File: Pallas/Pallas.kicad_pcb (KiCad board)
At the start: 2 copper layers, 467.5 x 140 mm, 263 parts, among them J1 OLED, J2 RGB_LED, Q1 IRLML6344TRPbF, SW00 SW_PUSH, SW01 SW_PUSH, SW010 SW_PUSH, SW011 SW_PUSH, SW012 SW_PUSH, SW013 SW_PUSH, SW014 SW_PUSH, SW02 SW_PUSH, SW03 SW_PUSH, SW04 SW_PUSH, SW05 SW_PUSH, SW06 SW_PUSH, SW07 SW_PUSH, SW08 SW_PUSH, SW09 SW_PUSH, SW10 SW_PUSH, SW11 SW_PUSH, SW110 SW_PUSH, SW111 SW_PUSH, SW112 SW_PUSH, SW113 SW_PUSH, SW114 SW_PUSH, SW12 SW_PUSH, SW13 SW_PUSH, SW14 SW_PUSH, SW15 SW_PUSH, SW16 SW_PUSH, SW17 SW_PUSH, SW18 SW_PUSH, SW19 SW_PUSH, SW20 SW_PUSH, SW21 SW_PUSH, SW210 SW_PUSH, SW211 SW_PUSH, SW212 SW_PUSH, SW213 SW_PUSH, SW214 SW_PUSH, SW22 SW_PUSH, SW23 SW_PUSH, SW24 SW_PUSH, SW25 SW_PUSH, SW26 SW_PUSH, SW27 SW_PUSH, SW28 SW_PUSH, SW29 SW_PUSH, SW30 SW_PUSH, SW31 SW_PUSH, SW310 SW_PUSH, SW311 SW_PUSH, SW312 SW_PUSH, SW313 SW_PUSH, SW314 SW_PUSH, SW32 SW_PUSH, SW33 SW_PUSH, SW34 SW_PUSH, SW35 SW_PUSH, SW36 SW_PUSH, SW37 SW_PUSH, SW38 SW_PUSH, SW39 SW_PUSH, SW40 SW_PUSH, SW41 SW_PUSH, SW410 SW_PUSH, SW411 SW_PUSH, SW412 SW_PUSH, SW413 SW_PUSH, SW414 SW_PUSH, SW42 SW_PUSH, SW43 SW_PUSH, SW44 SW_PUSH, SW45 SW_PUSH, SW46 SW_PUSH, SW47 SW_PUSH, SW48 SW_PUSH, SW49 SW_PUSH, U1 Elite-C

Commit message: Fix label switch label with stabs
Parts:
- renumbered DecorationHoleTop1 to DecorationHoleTop2

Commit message: Review diode and resistor position with stabs
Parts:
- moved R214 28.9 mm to (495.5, 104.1), turned to 270 degrees
- moved D30 27.0 mm to (73.0, 113.7), turned to 90 degrees
- moved R30 26.4 mm to (109.2, 103.6), turned to 270 degrees
- moved R44 26.3 mm to (214.3, 140.2), turned to 258 degrees
- moved D44 26.3 mm to (178.0, 142.6), turned to 78 degrees
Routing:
- net row3: track 600.4 -> 624.8 mm, vias 24 -> 26
- net Net-(R44-Pad2): track 7.64 -> 21.8 mm
- net Net-(R30-Pad2): track 7.24 -> 20.7 mm
- net row4: track 633.2 -> 623.7 mm
- net Net-(R214-Pad2): track 23.1 -> 32.0 mm
- net Net-(D30-Pad2): track 10.1 -> 18.4 mm
- net Net-(D44-Pad2): track 9.70 -> 17.8 mm
- net LED: track 2375.6 -> 2383.0 mm
- net VCC: track 2291.1 -> 2287.9 mm, vias 12 -> 10
- net GND: vias 2 -> 5

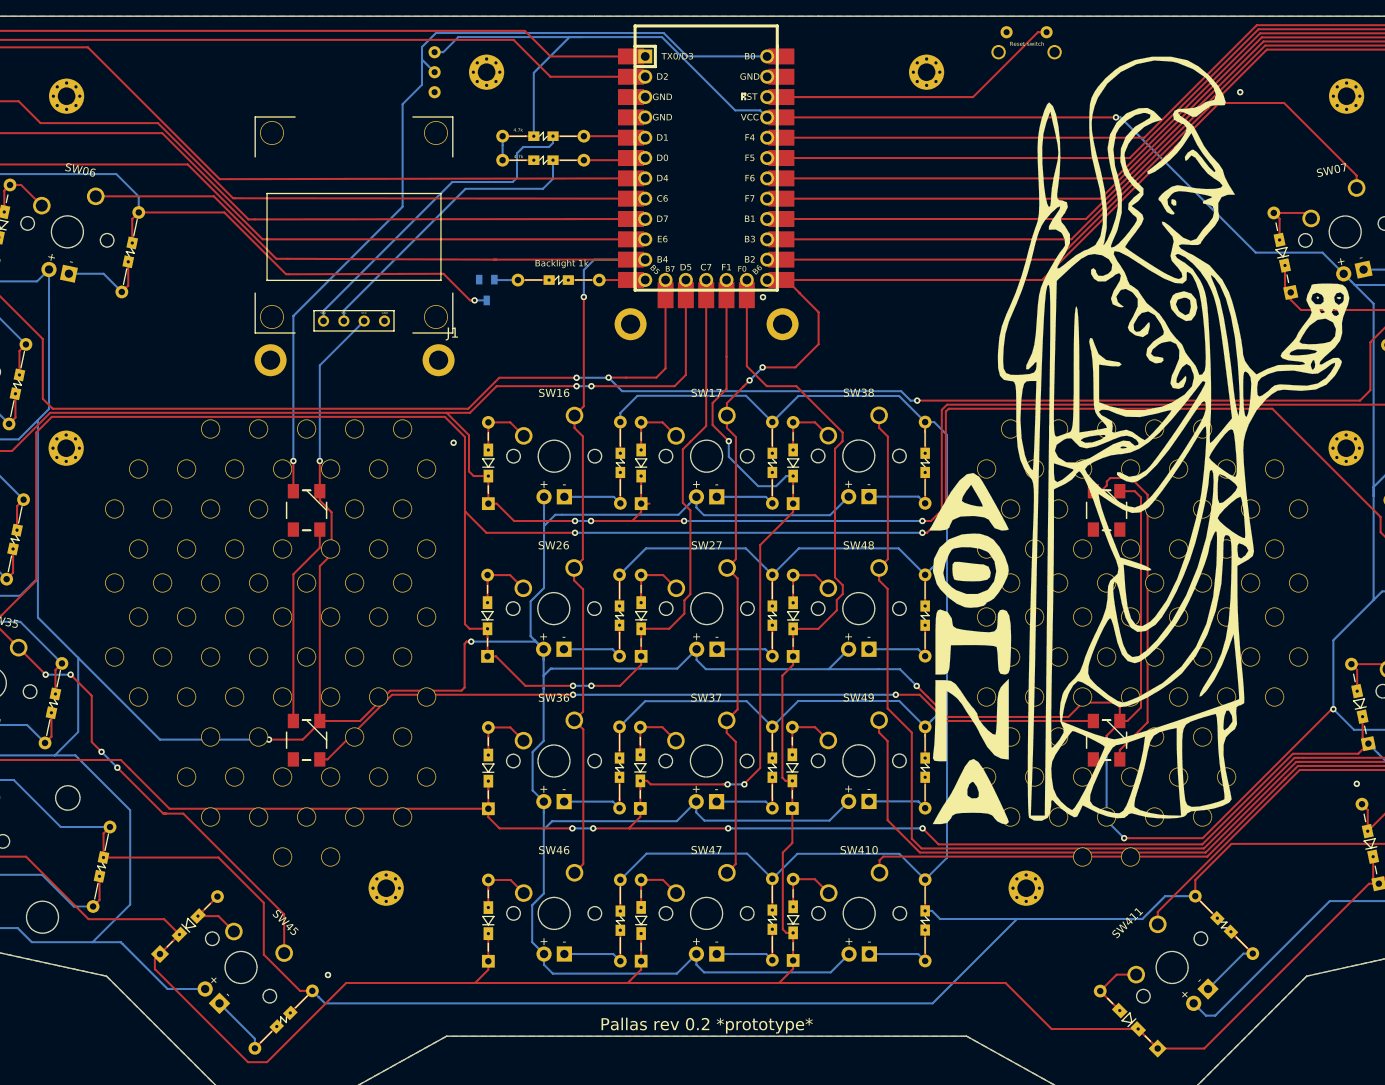
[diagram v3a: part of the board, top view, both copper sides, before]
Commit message: update RGB led footprint and route
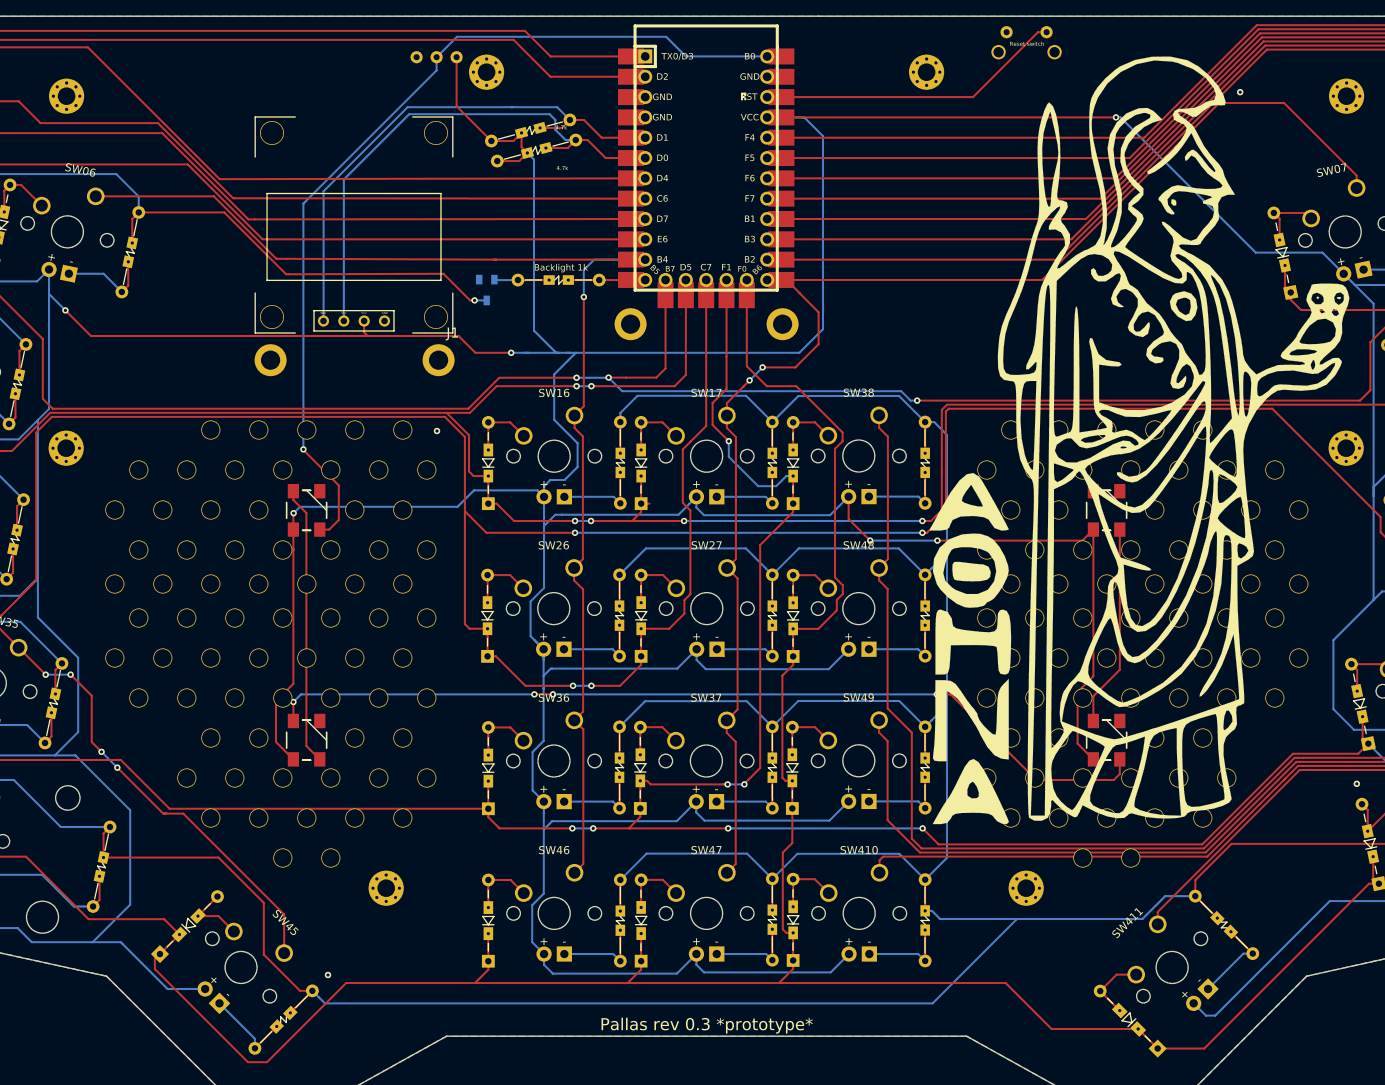
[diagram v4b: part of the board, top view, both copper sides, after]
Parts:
- moved J2 1.89 mm to (255.1, 44.0), turned to 0 degrees
- moved R1 1.52 mm to (262.0, 54.5), turned to 15 degrees
- moved R2 0.68 mm to (262.7, 57.0), turned to 15 degrees
- moved DecorationHoleTop1 0.13 mm to (238.9, 114.1)
- moved DecorationHoleTop2 0.13 mm to (338.9, 114.1)
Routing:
- net VCC: track 2287.9 -> 2309.2 mm, vias 10 -> 8
- net Net-(RGB3-Pad4): track 43.5 -> 25.3 mm
- net SCL: track 48.2 -> 64.5 mm
- net SDA: track 52.9 -> 65.2 mm
- net Net-(RGB2-Pad4): track 101.4 -> 112.6 mm, vias 2 -> 4
- net Net-(RGB1-Pad4): track 25.3 -> 34.9 mm
- net RGB: track 111.3 -> 114.7 mm
- net GND: track 3.05 -> 3.25 mm, vias 5 -> 4
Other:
- board text added: "Pallas rev 0.3 *prototype*"
- board text removed: "Pallas rev 0.2 *prototype*"
